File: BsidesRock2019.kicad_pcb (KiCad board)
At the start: 2 copper layers, 98.9 x 76 mm, 27 parts, among them U1 ATtiny85V-10SU

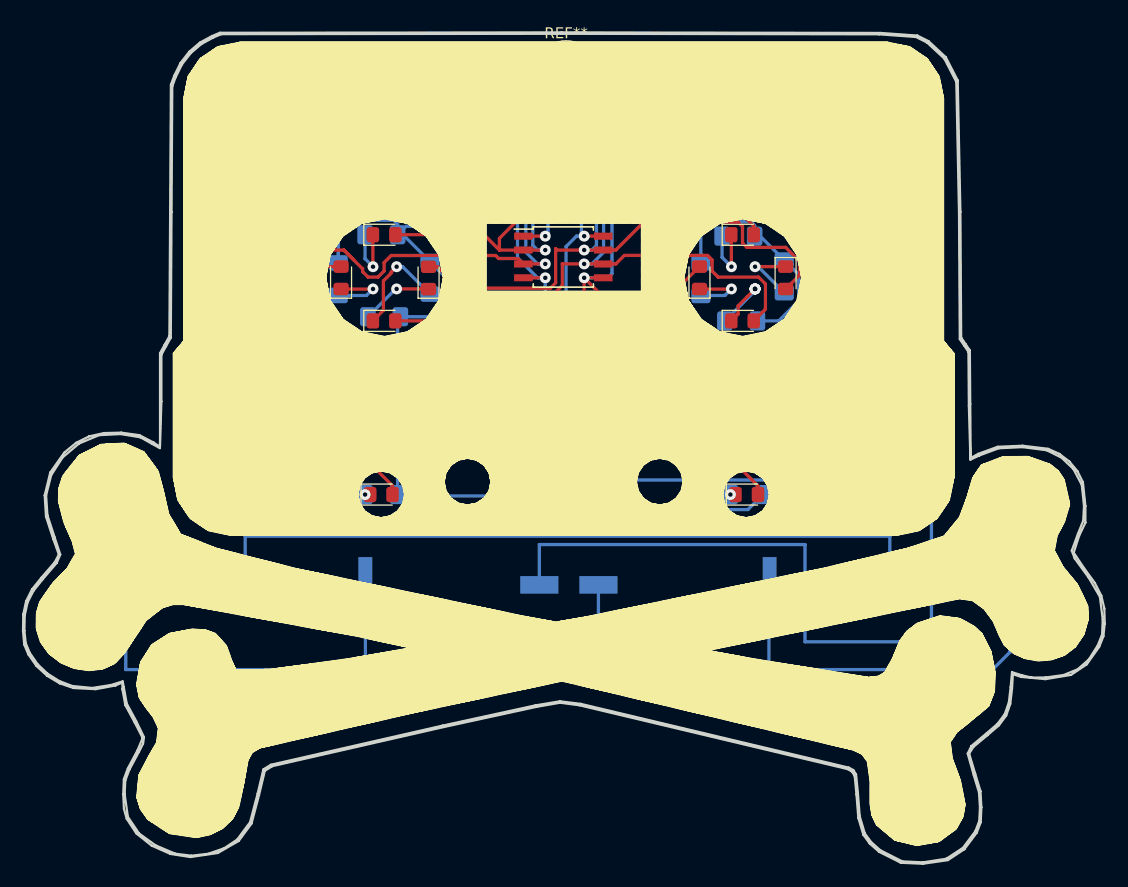
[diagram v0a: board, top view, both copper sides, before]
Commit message: Add files via upload
updated routes to pwn pins and ordered designs
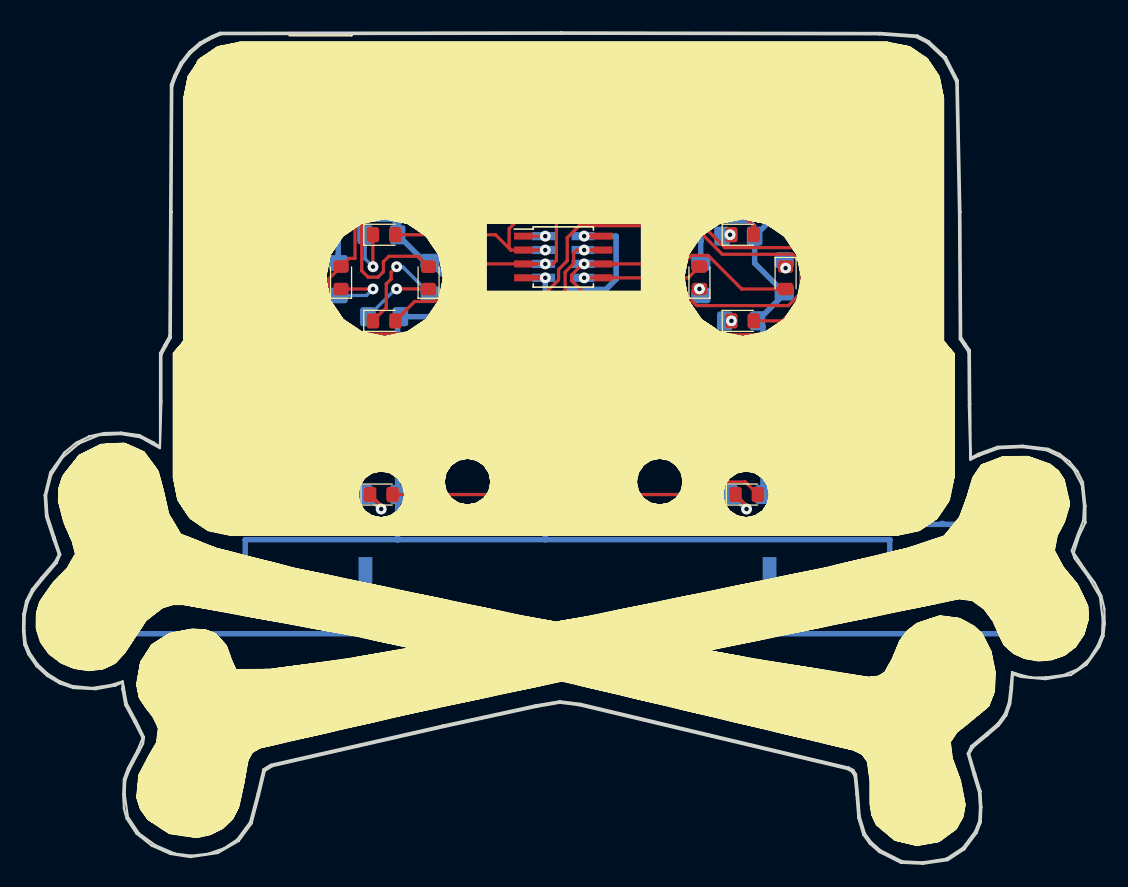
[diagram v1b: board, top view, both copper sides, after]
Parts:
- removed C100uF1: CP1_Small, Capacitor_SMD:CP_Elec_6.3x5.4_Nichicon
- removed JPROGHEADER1: Conn_01x08_Male, Connector_PinSocket_1.00mm:PinSocket_2x04_P1.00mm_Vertical_SMD
- removed REF**: TestPoint_Plated_Hole_D5.0mm, TestPoint:TestPoint_Plated_Hole_D5.0mm
- removed SW-LEDGROUND1: SW_SPST, Button_Switch_SMD:SW_SPST_EVQPE1
- added BLANKHOLE: TestPoint_Plated_Hole_D5.0mm, TestPoint:TestPoint_Plated_Hole_D5.0mm, F.Cu at (146.3, 41.9)
- added J2: #badgelife, Connector:Badgelife-Shitty-2x2, F.Cu at (115.5, 42.5)
- added J2: #badgelife, Connector:Badgelife-Shitty-2x2, F.Cu at (176.9, 42.4)
- added SMDPROGCONN: PinSocket_2x04_P1.27mm_Vertical_SMD, Connector_PinSocket_1.27mm:PinSocket_2x04_P1.27mm_Vertical_SMD, B.Cu at (146.1, 57.7)
- turned R56-Ohm10 to 270 degrees
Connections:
- R56-Ohm1 pad 2: Net-(R56-Ohm1-Pad2) -> Net-(BT-2032-1-Pad2)
- R56-Ohm10 pad 2: Net-(R56-Ohm1-Pad2) -> Net-(BT-2032-1-Pad2)
- R56-Ohm2 pad 2: Net-(R56-Ohm1-Pad2) -> Net-(BT-2032-1-Pad2)
- R56-Ohm3 pad 2: Net-(R56-Ohm1-Pad2) -> Net-(BT-2032-1-Pad2)
- R56-Ohm4 pad 2: Net-(R56-Ohm1-Pad2) -> Net-(BT-2032-1-Pad2)
- R56-Ohm5 pad 2: Net-(R56-Ohm1-Pad2) -> Net-(BT-2032-1-Pad2)
- R56-Ohm6 pad 2: Net-(R56-Ohm1-Pad2) -> Net-(BT-2032-1-Pad2)
- R56-Ohm7 pad 2: Net-(R56-Ohm1-Pad2) -> Net-(BT-2032-1-Pad2)
- R56-Ohm8 pad 2: Net-(R56-Ohm1-Pad2) -> Net-(BT-2032-1-Pad2)
- R56-Ohm9 pad 2: Net-(R56-Ohm1-Pad2) -> Net-(BT-2032-1-Pad2)
- U1 pad 3: Net-(D2-Pad2) -> Net-(D4-Pad2)
- U1 pad 6: Net-(D4-Pad2) -> Net-(D10-Pad2)
- U1 pad 7: Net-(D10-Pad2) -> Net-(D2-Pad2)
- U1 pad 8: Net-(C100uF1-Pad1) -> Net-(BT-2032-1-Pad1)
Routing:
- net Net-(BT-2032-1-Pad1): track 118.6 -> 291.4 mm, vias 0 -> 1
- net Net-(R56-Ohm1-Pad2): track 130.2 -> 0.00 mm
- net Net-(C100uF1-Pad1): track 126.2 -> 0.00 mm, vias 1 -> 0
- net Net-(D1-Pad2): track 70.0 -> 192.4 mm
- net Net-(BT-2032-1-Pad2): track 135.5 -> 236.8 mm
- net Net-(D10-Pad2): track 53.4 -> 150.4 mm
- net Net-(D2-Pad2): track 107.8 -> 61.0 mm
- net Net-(D3-Pad2): track 49.5 -> 41.7 mm
- net Net-(D8-Pad1): track 7.88 -> 0.61 mm, vias 3 -> 1
- net Net-(D10-Pad1): track 6.58 -> 0.91 mm
- net Net-(D6-Pad1): track 5.97 -> 0.66 mm
- net Net-(D7-Pad1): track 6.07 -> 0.90 mm
- net Net-(JPROGHEADER1-Pad2): track 6.45 -> 2.00 mm
- net Net-(D2-Pad1): track 0.00 -> 3.77 mm
- net Net-(D9-Pad1): track 0.00 -> 3.77 mm
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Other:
- net class power added: clearance 0.3, trace_width 0.5, via_dia 1, via_drill 0.4
- board text added: "++++++++++[>+>+++>+++++++>++++++++++<<<<-]>>>>--. +++++++++++++++++.----------.-----.+.++++++++++++ ++.<<++.>>-.---.------------.+++++.---.++++++++++ ++++.+.---------------.+++++++++++++.<<.+++++++++ +++++++++.--.+.++++++++.<++++++++++++++++++++++.> ------------.<++++++++++++++++++++++++++++++++.>> >--------.++++++++.+++++.-----."
- board text added: "0"
- board text added: "1"
- board text added: "2"
- board text added: "3"
- board text added: "4"
- board text added: "ATTiny85 ISP Programming Port"
- board text added: "Designed by: JRWR of Team Interlock Rochester"
- board text added: "GND"
- board text added: "RST"
- board text added: "Shitty Addon Port #BADGELIFE"
- board text added: "VCC"
